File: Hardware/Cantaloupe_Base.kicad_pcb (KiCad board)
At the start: 2 copper layers, 142.1 x 117 mm, 8 parts, among them SW33 Reset

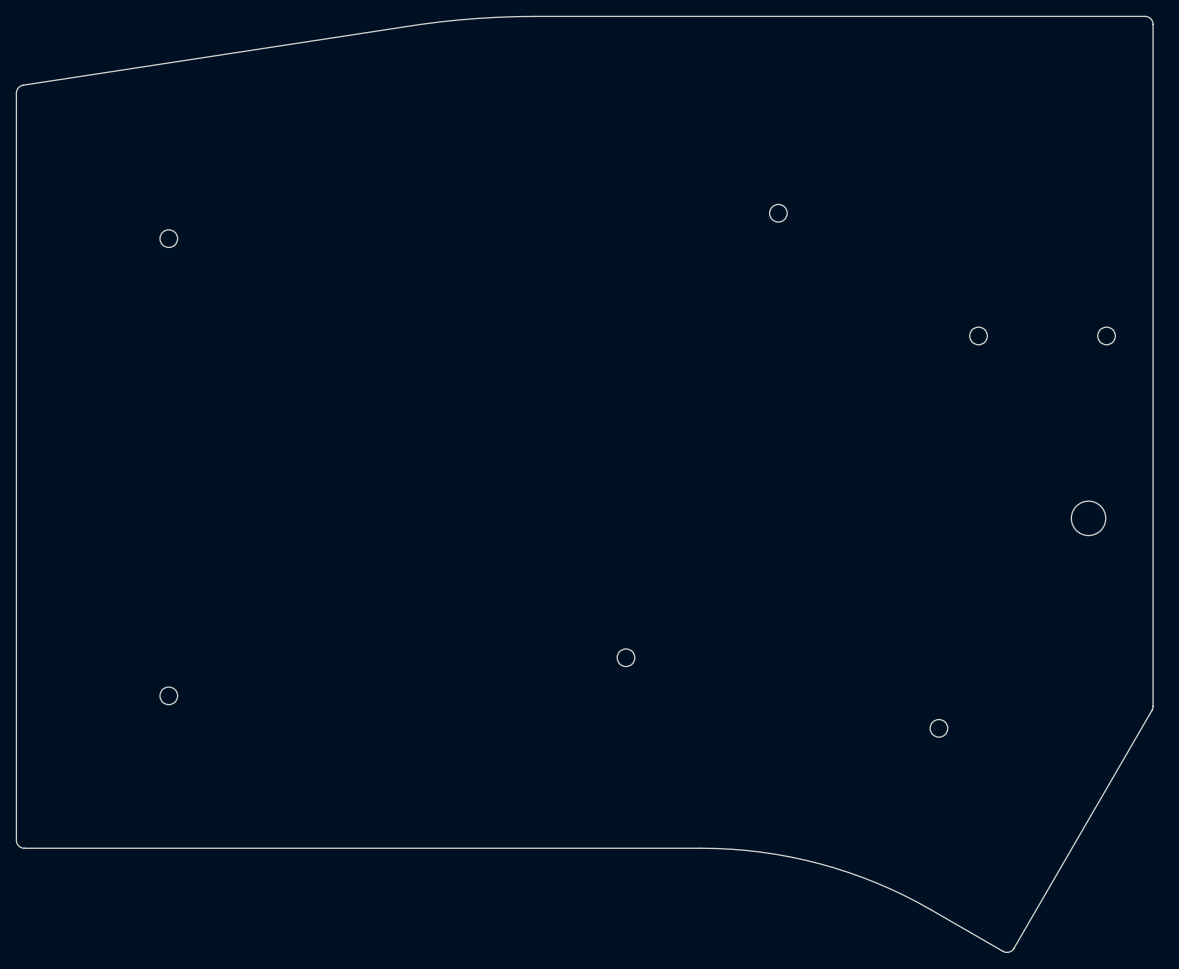
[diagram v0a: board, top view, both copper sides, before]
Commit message: Updated to V1.3.
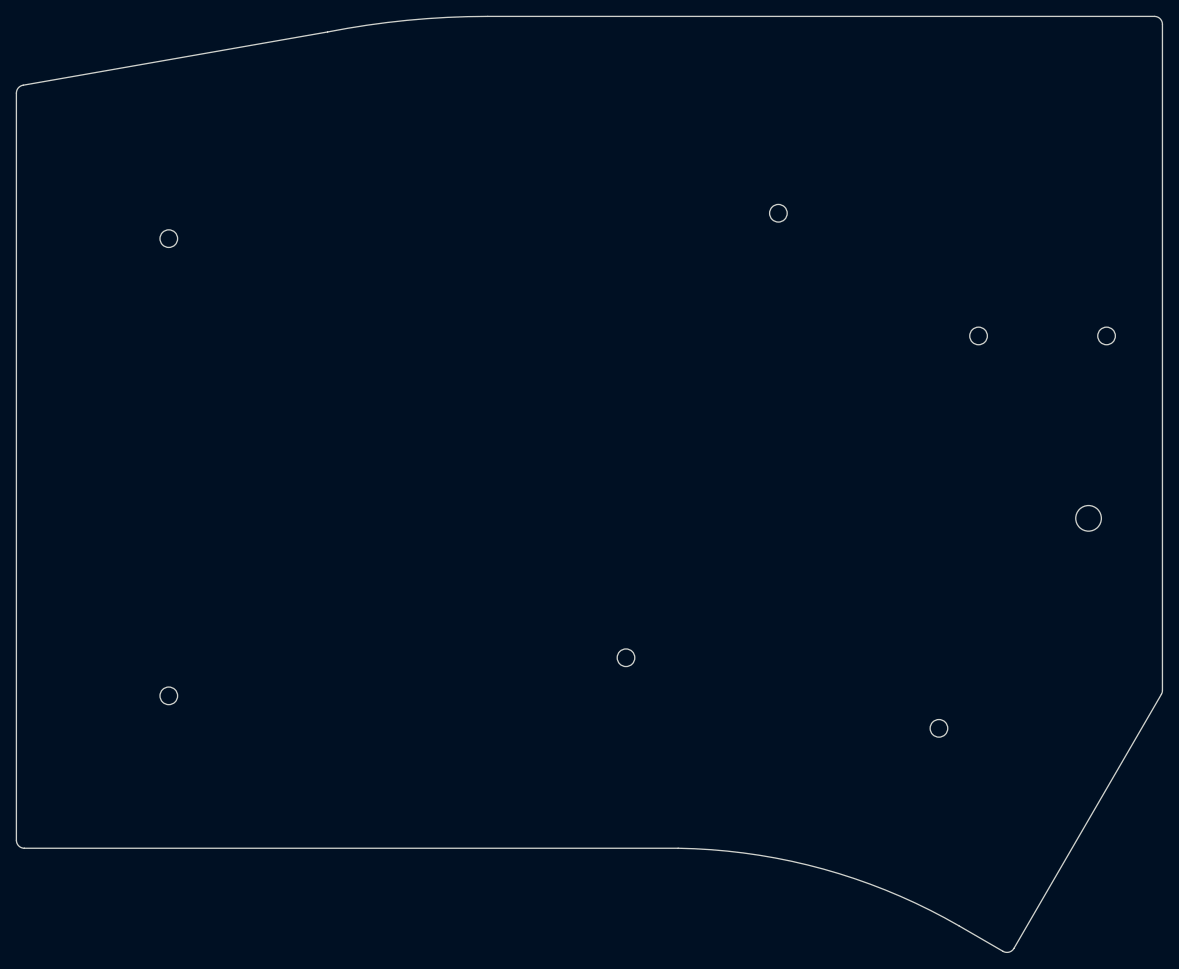
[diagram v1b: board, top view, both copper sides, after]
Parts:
- SW33: footprint MountingHole:MountingHole_4.3mm_M4 -> MountingHole:MountingHole_3.2mm_M3
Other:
- board size 142.1 x 117 mm -> 143.3 x 117 mm
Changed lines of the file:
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@@
       (drillshape 0)
       (scaleselection 1)
-      (outputdirectory "CantaloupeV1.1-Gerbers_Base/"))
+      (outputdirectory "CantaloupeV1.3-Gerbers_Base/"))
   )
   (net 0 "")
@@
     (uvia_drill 0.1)
   )
+  (module MountingHole:MountingHole_3.2mm_M3 (layer B.Cu)
+    (at 329.2825 95.287549 270)
+    (descr "Mounting Hole 3.2mm, no annular, M3")
+    (tags "mounting hole 3.2mm no annular m3")
+    (attr virtual)
+    (fp_text reference SW33 (at 0 3.75 90) (layer B.SilkS) hide
+      (effects (font (size 1 1) (thickness 0.15)) (justify mirror))
+    )
+    (fp_text value Reset (at 0 -3.75 90) (layer B.Fab)
+      (effects (font (size 1 1) (thickness 0.15)) (justify mirror))
+    )
+    (fp_text user %R (at 0 3.75 90) (layer B.Fab)
+      (effects (font (size 1 1) (thickness 0.15)) (justify mirror))
+    )
+    (fp_circle (center 0 0) (end 3.2 0) (layer Cmts.User) (width 0.15))
+    (fp_circle (center 0 0) (end 3.45 0) (layer B.CrtYd) (width 0.05))
+    (pad 1 np_thru_hole circle (at 0 0 270) (size 3.2 3.2) (drill 3.2) (layers *.Cu *.Mask)
+      (net 1 RESET))
+  )
   (module MountingHole:MountingHole_2.2mm_M2 (layer F.Cu)
     (at 331.5325 72.487549)
@@
       (effects (font (size 1 1) (thickness 0.15)))
     )
+    (fp_circle (center 0 0) (end 2.45 0) (layer F.CrtYd) (width 0.05))
+    (fp_circle (center 0 0) (end 2.2 0) (layer Cmts.User) (width 0.15))
     (fp_text user %R (at 0.3 0) (layer F.Fab)
       (effects (font (size 1 1) (thickness 0.15)))
     )
-    (fp_circle (center 0 0) (end 2.2 0) (layer Cmts.User) (width 0.15))
-    (fp_circle (center 0 0) (end 2.45 0) (layer F.CrtYd) (width 0.05))
     (pad 1 np_thru_hole circle (at 0 0) (size 2.2 2.2) (drill 2.2) (layers *.Cu *.Mask))
   )
@@
       (effects (font (size 1 1) (thickness 0.15)))
     )
+    (fp_circle (center 0 0) (end 2.45 0) (layer F.CrtYd) (width 0.05))
+    (fp_circle (center 0 0) (end 2.2 0) (layer Cmts.User) (width 0.15))
     (fp_text user %R (at 0.3 0) (layer F.Fab)
       (effects (font (size 1 1) (thickness 0.15)))
     )
-    (fp_circle (center 0 0) (end 2.2 0) (layer Cmts.User) (width 0.15))
-    (fp_circle (center 0 0) (end 2.45 0) (layer F.CrtYd) (width 0.05))
     (pad 1 np_thru_hole circle (at 0 0) (size 2.2 2.2) (drill 2.2) (layers *.Cu *.Mask))
-  )
-  (module MountingHole:MountingHole_4.3mm_M4 (layer B.Cu)
-    (at 329.2825 95.287549 270)
-    (descr "Mounting Hole 4.3mm, no annular, M4")
-    (tags "mounting hole 4.3mm no annular m4")
-    (attr virtual)
-    (fp_text reference SW33 (at 0 3.75 90) (layer B.SilkS) hide
-      (effects (font (size 1 1) (thickness 0.15)) (justify mirror))
-    )
-    (fp_text value Reset (at 0 -3.75 90) (layer B.Fab)
-      (effects (font (size 1 1) (thickness 0.15)) (justify mirror))
-    )
-    (fp_circle (center 0 0) (end 4.3 0) (layer Cmts.User) (width 0.15))
-    (fp_circle (center 0 0) (end 4.55 0) (layer B.CrtYd) (width 0.05))
-    (fp_text user %R (at 0 3.75 90) (layer B.Fab)
-      (effects (font (size 1 1) (thickness 0.15)) (justify mirror))
-    )
-    (pad 1 np_thru_hole circle (at 0 0 270) (size 4.3 4.3) (drill 4.3) (layers *.Cu *.Mask)
-      (net 1 RESET))
   )
   (module MountingHole:MountingHole_2.2mm_M2 (layer F.Cu)
@@
       (effects (font (size 1 1) (thickness 0.15)))
     )
+    (fp_circle (center 0 0) (end 2.45 0) (layer F.CrtYd) (width 0.05))
     (fp_circle (center 0 0) (end 2.2 0) (layer Cmts.User) (width 0.15))
-    (fp_circle (center 0 0) (end 2.45 0) (layer F.CrtYd) (width 0.05))
     (fp_text user %R (at 0.3 0) (layer F.Fab)
       (effects (font (size 1 1) (thickness 0.15)))
@@
       (effects (font (size 1 1) (thickness 0.15)))
     )
+    (fp_circle (center 0 0) (end 2.45 0) (layer F.CrtYd) (width 0.05))
     (fp_circle (center 0 0) (end 2.2 0) (layer Cmts.User) (width 0.15))
-    (fp_circle (center 0 0) (end 2.45 0) (layer F.CrtYd) (width 0.05))
     (fp_text user %R (at 0.3 0) (layer F.Fab)
       (effects (font (size 1 1) (thickness 0.15)))
@@
       (effects (font (size 1 1) (thickness 0.15)))
     )
+    (fp_circle (center 0 0) (end 2.45 0) (layer F.CrtYd) (width 0.05))
     (fp_circle (center 0 0) (end 2.2 0) (layer Cmts.User) (width 0.15))
-    (fp_circle (center 0 0) (end 2.45 0) (layer F.CrtYd) (width 0.05))
     (fp_text user %R (at 0.3 0) (layer F.Fab)
       (effects (font (size 1 1) (thickness 0.15)))
@@
       (effects (font (size 1 1) (thickness 0.15)))
     )
+    (fp_circle (center 0 0) (end 2.45 0) (layer F.CrtYd) (width 0.05))
     (fp_circle (center 0 0) (end 2.2 0) (layer Cmts.User) (width 0.15))
-    (fp_circle (center 0 0) (end 2.45 0) (layer F.CrtYd) (width 0.05))
     (fp_text user %R (at 0.3 0) (layer F.Fab)
       (effects (font (size 1 1) (thickness 0.15)))
@@
       (effects (font (size 1 1) (thickness 0.15)))
     )
+    (fp_circle (center 0 0) (end 2.45 0) (layer F.CrtYd) (width 0.05))
     (fp_circle (center 0 0) (end 2.2 0) (layer Cmts.User) (width 0.15))
-    (fp_circle (center 0 0) (end 2.45 0) (layer F.CrtYd) (width 0.05))
     (fp_text user %R (at 0.3 0) (layer F.Fab)
       (effects (font (size 1 1) (thickness 0.15)))
@@
     (pad 1 np_thru_hole circle (at 0 0) (size 2.2 2.2) (drill 2.2) (layers *.Cu *.Mask))
   )
-  (gr_line (start 196.111473 41.145343) (end 245.712142 33.556686) (layer Edge.Cuts) (width 0.1))
-  (gr_line (start 260.188449 32.543749) (end 336.343499 32.543749) (layer Edge.Cuts) (width 0.1))
-  (gr_arc (start 260.188449 136.493749) (end 260.188449 32.543749) (angle -8.005156052) (layer Edge.Cuts) (width 0.1))
-  (gr_arc (start 280.8825 193.925049) (end 280.8325 136.525049) (angle 30.02255225) (layer Edge.Cuts) (width 0.1))
-  (gr_line (start 318.5893 149.409776) (end 309.558773 144.201474) (layer Edge.Cuts) (width 0.1))
+  (gr_line (start 196.111473 41.145343) (end 234.165535 34.49046) (layer Edge.Cuts) (width 0.1))
+  (gr_arc (start 254.188807 136.493749) (end 254.188807 32.543749) (angle -11.10596181) (layer Edge.Cuts) (width 0.1))
+  (gr_line (start 254.188807 32.543749) (end 337.518492 32.543746) (layer Edge.Cuts) (width 0.1))
+  (gr_line (start 338.518495 33.543751) (end 338.518495 116.786264) (layer Edge.Cuts) (width 0.1))
+  (gr_arc (start 337.518491 33.54375) (end 337.518492 32.543746) (angle 90) (layer Edge.Cuts) (width 0.1))
+  (gr_arc (start 337.518501 116.786264) (end 338.383042 117.288823) (angle -30.16947172) (layer Edge.Cuts) (width 0.1))
+  (gr_line (start 338.383042 117.288823) (end 319.955326 149.043748) (layer Edge.Cuts) (width 0.1))
+  (gr_arc (start 276.852497 209.000096) (end 277.982499 136.525048) (angle 29.07937341) (layer Edge.Cuts) (width 0.1))
+  (gr_line (start 318.589299 149.409775) (end 313.064439 146.209932) (layer Edge.Cuts) (width 0.1))
+  (gr_line (start 277.982499 136.525048) (end 196.262499 136.525048) (layer Edge.Cuts) (width 0.1))
   (gr_arc (start 319.089299 148.54375) (end 318.5893 149.409776) (angle -90) (layer Edge.Cuts) (width 0.1))
-  (gr_line (start 337.208042 119.295073) (end 319.955325 149.043749) (layer Edge.Cuts) (width 0.1))
-  (gr_line (start 337.3435 33.543748) (end 337.3435 118.792514) (layer Edge.Cuts) (width 0.1))
-  (gr_arc (start 336.3435 33.543749) (end 337.3435 33.543748) (angle -90) (layer Edge.Cuts) (width 0.1))
   (gr_arc (start 196.262499 135.525049) (end 195.2625 135.525049) (angle -90) (layer Edge.Cuts) (width 0.1))
-  (gr_line (start 280.8325 136.525049) (end 196.2625 136.525049) (layer Edge.Cuts) (width 0.1))
   (gr_line (start 195.2625 135.525049) (end 195.2625 42.133874) (layer Edge.Cuts) (width 0.1))
-  (gr_arc (start 336.3435 118.792514) (end 337.208042 119.295073) (angle -30.16947172) (layer Edge.Cuts) (width 0.1))
   (gr_arc (start 196.2625 42.133873) (end 196.111473 41.145343) (angle -81.31359643) (layer Edge.Cuts) (width 0.1))
 )

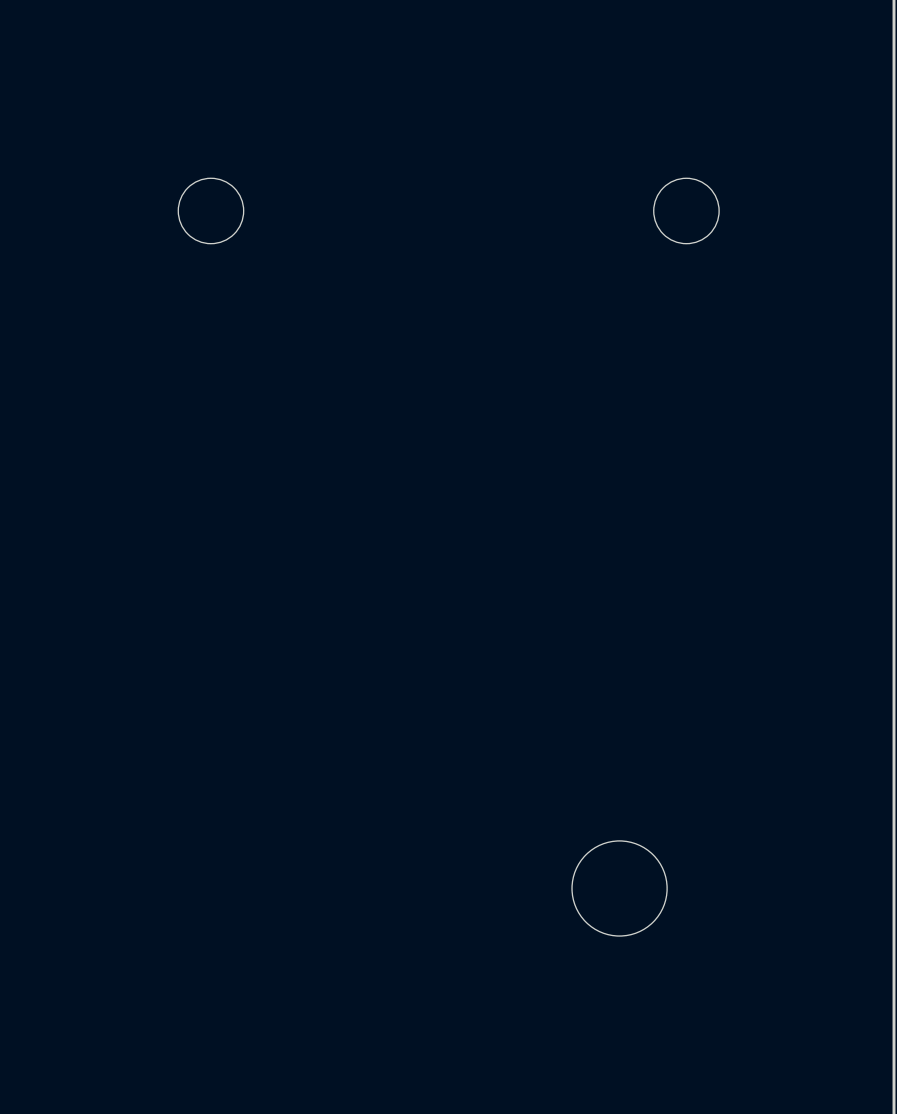
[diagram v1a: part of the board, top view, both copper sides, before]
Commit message: Changed OLED support to 0.96" OLED
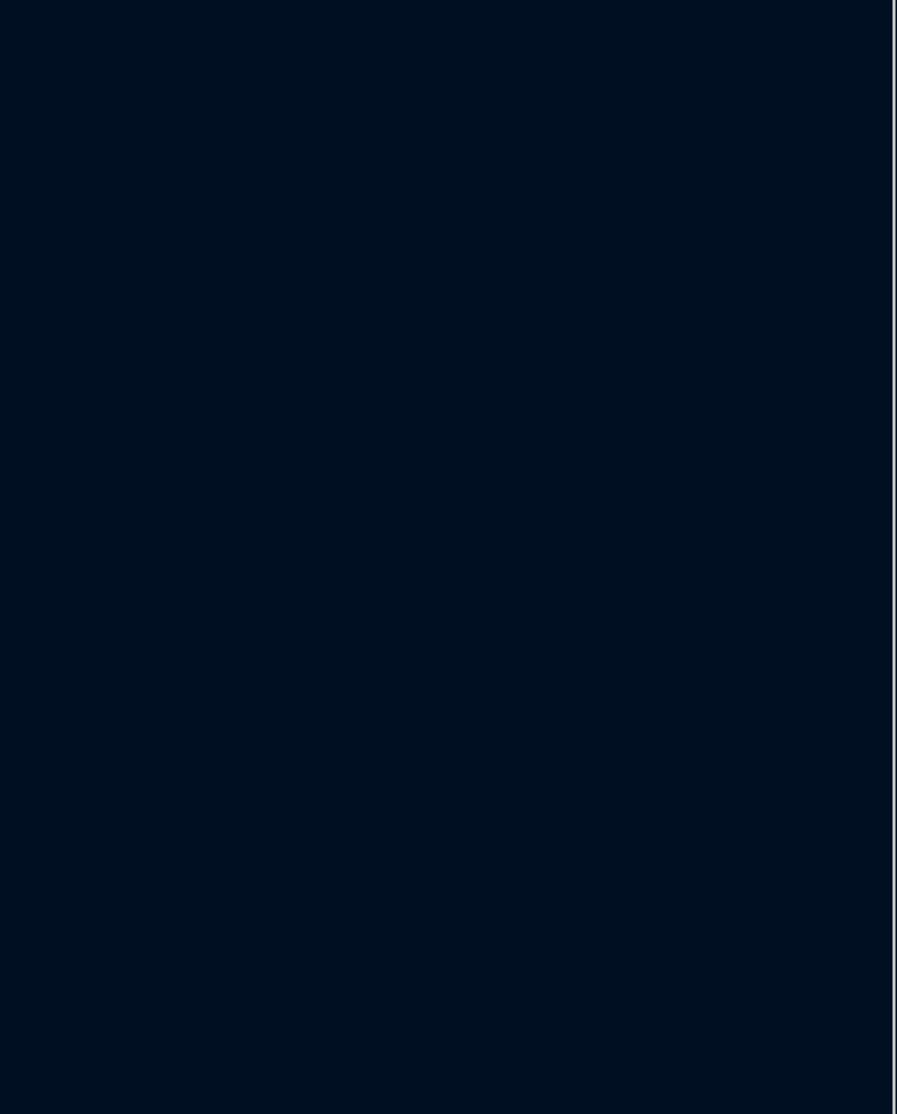
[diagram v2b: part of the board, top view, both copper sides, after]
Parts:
- removed the REF** at (331.5, 72.5)
- removed the REF** at (315.5, 72.5)
- removed SW33: Reset, MountingHole:MountingHole_3.2mm_M3
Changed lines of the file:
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@@
     (tracks 0)
     (zones 0)
-    (modules 8)
-    (nets 2)
+    (modules 5)
+    (nets 1)
   )
   (page A3)
@@
   )
   (net 0 "")
-  (net 1 RESET)
   (net_class Default "This is the default net class."
     (clearance 0.2)
@@
     (uvia_dia 0.3)
     (uvia_drill 0.1)
-    (add_net RESET)
   )
   (net_class Battery ""
@@
     (uvia_drill 0.1)
   )
-  (module MountingHole:MountingHole_3.2mm_M3 (layer B.Cu)
-    (at 329.2825 95.287549 270)
-    (descr "Mounting Hole 3.2mm, no annular, M3")
-    (tags "mounting hole 3.2mm no annular m3")
-    (attr virtual)
-    (fp_text reference SW33 (at 0 3.75 90) (layer B.SilkS) hide
-      (effects (font (size 1 1) (thickness 0.15)) (justify mirror))
-    )
-    (fp_text value Reset (at 0 -3.75 90) (layer B.Fab)
-      (effects (font (size 1 1) (thickness 0.15)) (justify mirror))
-    )
-    (fp_text user %R (at 0 3.75 90) (layer B.Fab)
-      (effects (font (size 1 1) (thickness 0.15)) (justify mirror))
-    )
-    (fp_circle (center 0 0) (end 3.2 0) (layer Cmts.User) (width 0.15))
-    (fp_circle (center 0 0) (end 3.45 0) (layer B.CrtYd) (width 0.05))
-    (pad 1 np_thru_hole circle (at 0 0 270) (size 3.2 3.2) (drill 3.2) (layers *.Cu *.Mask)
-      (net 1 RESET))
-  )
-  (module MountingHole:MountingHole_2.2mm_M2 (layer F.Cu)
-    (at 331.5325 72.487549)
-    (descr "Mounting Hole 2.2mm, no annular, M2")
-    (tags "mounting hole 2.2mm no annular m2")
-    (attr virtual)
-    (fp_text reference REF** (at 0 -3.2) (layer F.SilkS) hide
-      (effects (font (size 1 1) (thickness 0.15)))
-    )
-    (fp_text value MountingHole_2.2mm_M2 (at 0 3.2) (layer F.Fab)
-      (effects (font (size 1 1) (thickness 0.15)))
-    )
-    (fp_circle (center 0 0) (end 2.45 0) (layer F.CrtYd) (width 0.05))
-    (fp_circle (center 0 0) (end 2.2 0) (layer Cmts.User) (width 0.15))
-    (fp_text user %R (at 0.3 0) (layer F.Fab)
-      (effects (font (size 1 1) (thickness 0.15)))
-    )
-    (pad 1 np_thru_hole circle (at 0 0) (size 2.2 2.2) (drill 2.2) (layers *.Cu *.Mask))
-  )
-  (module MountingHole:MountingHole_2.2mm_M2 (layer F.Cu)
-    (at 315.5325 72.487549)
-    (descr "Mounting Hole 2.2mm, no annular, M2")
-    (tags "mounting hole 2.2mm no annular m2")
-    (attr virtual)
-    (fp_text reference REF** (at 0 -3.2) (layer F.SilkS) hide
-      (effects (font (size 1 1) (thickness 0.15)))
-    )
-    (fp_text value MountingHole_2.2mm_M2 (at 0 3.2) (layer F.Fab)
-      (effects (font (size 1 1) (thickness 0.15)))
-    )
-    (fp_circle (center 0 0) (end 2.45 0) (layer F.CrtYd) (width 0.05))
-    (fp_circle (center 0 0) (end 2.2 0) (layer Cmts.User) (width 0.15))
-    (fp_text user %R (at 0.3 0) (layer F.Fab)
-      (effects (font (size 1 1) (thickness 0.15)))
-    )
-    (pad 1 np_thru_hole circle (at 0 0) (size 2.2 2.2) (drill 2.2) (layers *.Cu *.Mask))
-  )
   (module MountingHole:MountingHole_2.2mm_M2 (layer F.Cu)
     (at 310.58125 121.5375)
@@
       (effects (font (size 1 1) (thickness 0.15)))
     )
+    (fp_circle (center 0 0) (end 2.2 0) (layer Cmts.User) (width 0.15))
     (fp_circle (center 0 0) (end 2.45 0) (layer F.CrtYd) (width 0.05))
-    (fp_circle (center 0 0) (end 2.2 0) (layer Cmts.User) (width 0.15))
     (fp_text user %R (at 0.3 0) (layer F.Fab)
       (effects (font (size 1 1) (thickness 0.15)))
@@
       (effects (font (size 1 1) (thickness 0.15)))
     )
+    (fp_circle (center 0 0) (end 2.2 0) (layer Cmts.User) (width 0.15))
     (fp_circle (center 0 0) (end 2.45 0) (layer F.CrtYd) (width 0.05))
-    (fp_circle (center 0 0) (end 2.2 0) (layer Cmts.User) (width 0.15))
     (fp_text user %R (at 0.3 0) (layer F.Fab)
       (effects (font (size 1 1) (thickness 0.15)))
@@
       (effects (font (size 1 1) (thickness 0.15)))
     )
+    (fp_circle (center 0 0) (end 2.2 0) (layer Cmts.User) (width 0.15))
     (fp_circle (center 0 0) (end 2.45 0) (layer F.CrtYd) (width 0.05))
-    (fp_circle (center 0 0) (end 2.2 0) (layer Cmts.User) (width 0.15))
     (fp_text user %R (at 0.3 0) (layer F.Fab)
       (effects (font (size 1 1) (thickness 0.15)))
@@
       (effects (font (size 1 1) (thickness 0.15)))
     )
+    (fp_circle (center 0 0) (end 2.2 0) (layer Cmts.User) (width 0.15))
     (fp_circle (center 0 0) (end 2.45 0) (layer F.CrtYd) (width 0.05))
-    (fp_circle (center 0 0) (end 2.2 0) (layer Cmts.User) (width 0.15))
     (fp_text user %R (at 0.3 0) (layer F.Fab)
       (effects (font (size 1 1) (thickness 0.15)))
@@
       (effects (font (size 1 1) (thickness 0.15)))
     )
+    (fp_circle (center 0 0) (end 2.2 0) (layer Cmts.User) (width 0.15))
     (fp_circle (center 0 0) (end 2.45 0) (layer F.CrtYd) (width 0.05))
-    (fp_circle (center 0 0) (end 2.2 0) (layer Cmts.User) (width 0.15))
     (fp_text user %R (at 0.3 0) (layer F.Fab)
       (effects (font (size 1 1) (thickness 0.15)))
